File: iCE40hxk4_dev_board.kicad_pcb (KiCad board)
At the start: 4 copper layers, 66.4 x 162.5 mm, 365 parts, among them J1001 Testpoint, J1002 Testpoint, J1003 Testpoint, J1004 Testpoint, J1005 USB_EXT, J101 CONN_01X02, J102 NRJ6HM-1, J103 CONN_COAXIAL, J104 CONN_COAXIAL, J1101 CONN_01X25, J202 USB_OTG, J401 Testpoint, J402 Testpoint, J404 Testpoint, J405 Testpoint, J406 Testpoint, J501 Testpoint, J502 Testpoint, J601 CONN_01X02, J602 CONN_01X02, J603 Testpoint, J604 Testpoint, J605 Testpoint, J701 Testpoint, J703 Testpoint, J704 Testpoint, J705 Testpoint, J706 Testpoint, J801 Testpoint, J802 Testpoint, J803 Testpoint, J804 Testpoint, J805 Testpoint, J806 Testpoint, J807 Testpoint, J808 Testpoint, J809 Testpoint, J810 Testpoint, SW1101 SW_Push, U1001 ADC1175, U1002 ADC1175, U1101 MIC7300, U1102 MIC7300, U1103 MCP4716, U1104 MCP4716, U1105 MIC7300, U1106 MIC7300, U201 MIC2005A-2YM5, U203 93LC56BT-I/O, U204 MIC5355/6-xYMME, U205 FT2232H, U301 iCE40-HX4K-TQ144, U302 25LC_EEPROM, U501 AS4C1M16S, U701 CPC1017N, U702 CPC1017N, U703 CD4051BM96, U704 CD4051BM96, U801 CD4051BM96, U802 CD4051BM96, U803 CLC4007, U901 LM2776DBVR, U902 TCR2EF13, U903 MIC5270

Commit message: DRC
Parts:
- added J403, J702: Testpoint, library:TestPoint, F.Cu at (120.7, 200.2)
- J1001, J1002, J1003, J1004, J401, J402, J404, J405, J406, J501, J502, J603, J604, J605, J701, J703, J704, J705, J706, J801, J802, J803, J804, J805, J806, J807, J808, J809, J810: footprint library:Via-0.8mm -> library:TestPoint
- moved J405 136.3 mm to (102.9, 65.4)
- moved J406 126.5 mm to (107.8, 74.8)
- moved J501 115.0 mm to (137.9, 87.3)
- moved J502 111.6 mm to (102.6, 90.4)
- moved J1001 87.9 mm to (174.3, 132.6)
- moved J1002 87.9 mm to (174.3, 132.6)
- moved J1003 87.9 mm to (174.3, 132.6)
- moved J1004 87.9 mm to (174.3, 132.6)
- moved J603 87.9 mm to (174.3, 132.6)
- moved J604 87.9 mm to (174.3, 132.6)
- moved J605 87.9 mm to (174.3, 132.6)
- moved J701 87.9 mm to (174.3, 132.6)
- moved J703 87.9 mm to (174.3, 132.6)
- moved J704 87.9 mm to (174.3, 132.6)
- moved J705 87.9 mm to (174.3, 132.6)
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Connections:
- J1005 pad 2: Net-(J1005-Pad2) -> (no net)
- J1005 pad 3: Net-(J1005-Pad3) -> (no net)
- J1005 pad 4: Net-(J1005-Pad4) -> (no net)
- J202 pad 4: Net-(J202-Pad4) -> (no net)
- U1001 pad 16: Net-(U1001-Pad16) -> (no net)
- U1001 pad 22: Net-(U1001-Pad22) -> (no net)
- U1002 pad 16: Net-(U1002-Pad16) -> (no net)
- U1002 pad 22: Net-(U1002-Pad22) -> (no net)
- U205 pad 19: Net-(U205-Pad19) -> (no net)
- U205 pad 22: Net-(U205-Pad22) -> (no net)
- U205 pad 26: Net-(U205-Pad26) -> (no net)
- U205 pad 27: Net-(U205-Pad27) -> (no net)
- U205 pad 28: Net-(U205-Pad28) -> (no net)
- U205 pad 29: Net-(U205-Pad29) -> (no net)
- U205 pad 3: Net-(U205-Pad3) -> (no net)
- U205 pad 30: Net-(U205-Pad30) -> (no net)
- U205 pad 32: Net-(U205-Pad32) -> (no net)
- U205 pad 33: Net-(U205-Pad33) -> (no net)
- U205 pad 34: Net-(U205-Pad34) -> (no net)
- U205 pad 36: Net-(U205-Pad36) -> (no net)
- U205 pad 57: Net-(U205-Pad57) -> (no net)
- U205 pad 58: Net-(U205-Pad58) -> (no net)
- U205 pad 59: Net-(U205-Pad59) -> (no net)
- U205 pad 60: Net-(U205-Pad60) -> (no net)
- U301 pad 109: Net-(U301-Pad109) -> (no net)
- U301 pad 133: Net-(U301-Pad133) -> (no net)
- U301 pad 35: Net-(U301-Pad35) -> (no net)
- U301 pad 36: Net-(U301-Pad36) -> (no net)
- U301 pad 50: Net-(U301-Pad50) -> (no net)
- U301 pad 51: Net-(U301-Pad51) -> (no net)
- U301 pad 58: Net-(U301-Pad58) -> (no net)
- U301 pad 77: Net-(U301-Pad77) -> (no net)
- U501 pad 33: Net-(U501-Pad33) -> (no net)
- U501 pad 37: Net-(U501-Pad37) -> (no net)
- U902 pad 4: Net-(U902-Pad4) -> (no net)
- U903 pad 1: Net-(U903-Pad1) -> (no net)
- U903 pad 3: Net-(U903-Pad3) -> (no net)
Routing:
- net (no net): track 6.10 -> 0.19 mm
- net GND: track 1645.2 -> 1640.3 mm
- net +3V3: track 502.7 -> 498.3 mm
- net Net-(U205-Pad28): track 4.20 -> 0.00 mm
- net Net-(U205-Pad27): track 3.50 -> 0.00 mm
- net Net-(U205-Pad26): track 2.60 -> 0.00 mm
- net /Analog front end/ATTENUATION/CHB_ATT_40dB: track 36.0 -> 34.0 mm
- net /Analog front end/ATTENUATION/CHB_ATT_20dB: track 51.0 -> 49.2 mm
- net /Analog front end/CHB_PGA_OUT: track 45.4 -> 46.9 mm
- net /Analog front end/CHA_ATT_OUT: track 42.5 -> 43.8 mm
- net /Analog front end/CHB_ATT_OUT: track 57.3 -> 58.5 mm
- net /Analog front end/CHA_PGA_OUT: track 66.6 -> 67.3 mm

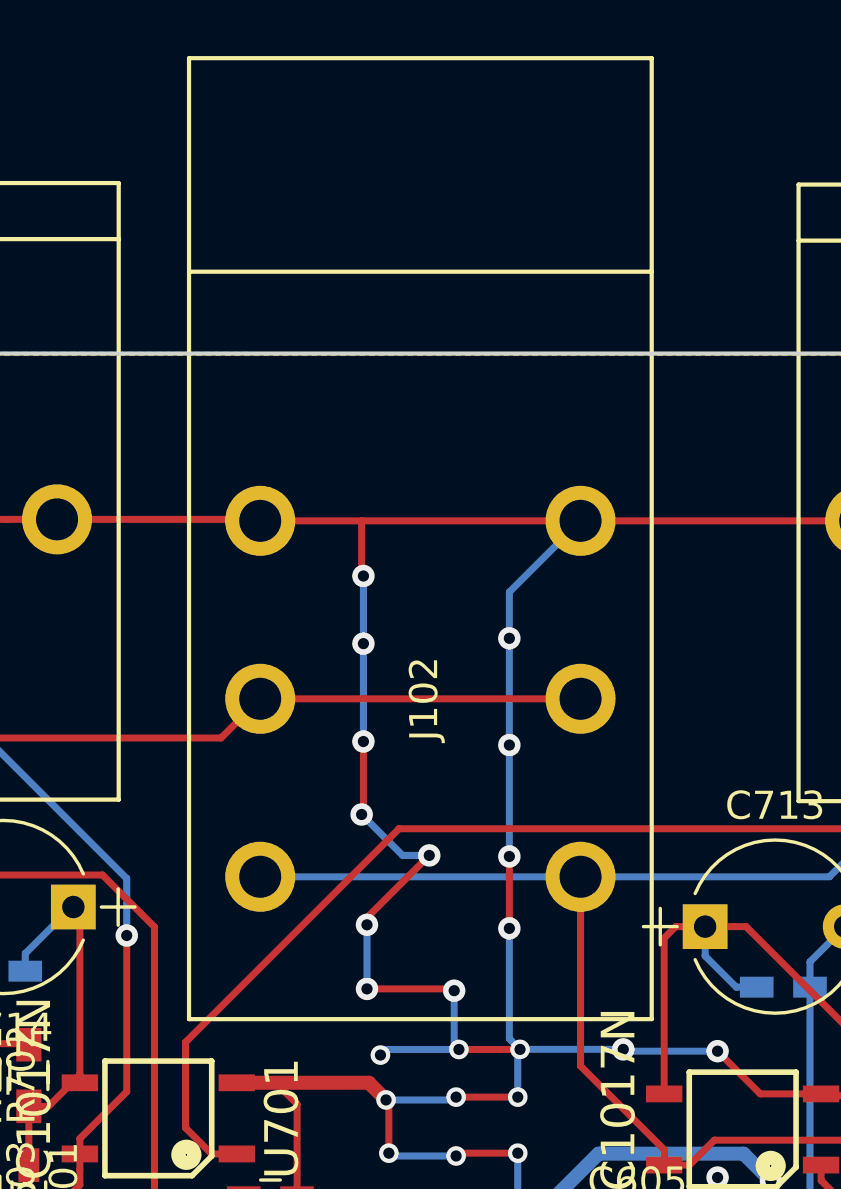
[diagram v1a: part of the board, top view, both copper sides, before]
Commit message: Changed 1/4 jack to 1/8 jack
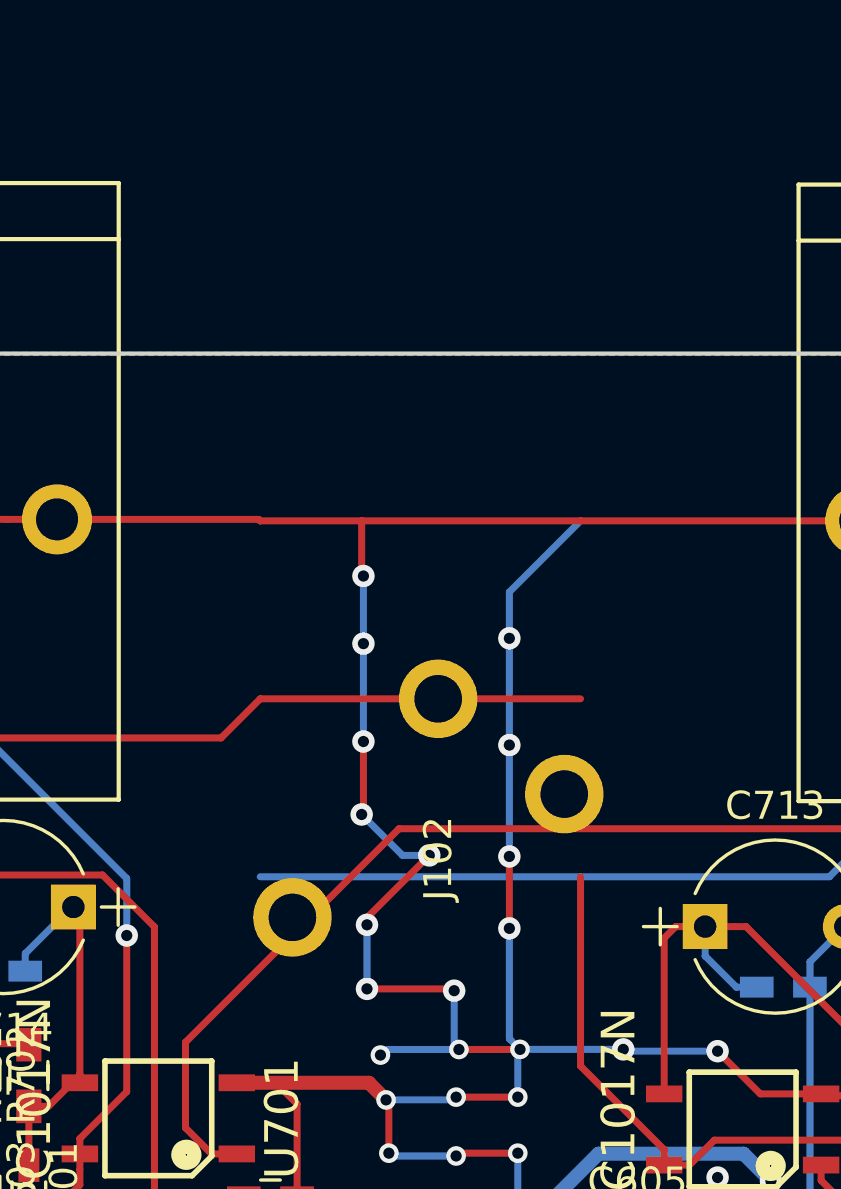
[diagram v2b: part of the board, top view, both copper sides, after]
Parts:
- J102: value NRJ6HM-1 -> KobiConn_161-3507_Jack_3.5mm; footprint library:NRJ6HM-1_audio_jack -> library:KobiConn_161-3507_Jack_3.5mm
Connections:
- J1005 pad 2: (no net) -> Net-(J1005-Pad2)
- J1005 pad 3: (no net) -> Net-(J1005-Pad3)
- J1005 pad 4: (no net) -> Net-(J1005-Pad4)
- J102 pad 2: /CHB -> /CHA
- J102 pad 3: /CHA -> /CHB
- J202 pad 4: (no net) -> Net-(J202-Pad4)
- U1001 pad 16: (no net) -> Net-(U1001-Pad16)
- U1001 pad 22: (no net) -> Net-(U1001-Pad22)
- U1002 pad 16: (no net) -> Net-(U1002-Pad16)
- U1002 pad 22: (no net) -> Net-(U1002-Pad22)
- U205 pad 19: (no net) -> Net-(U205-Pad19)
- U205 pad 22: (no net) -> Net-(U205-Pad22)
- U205 pad 26: (no net) -> Net-(U205-Pad26)
- U205 pad 27: (no net) -> Net-(U205-Pad27)
- U205 pad 28: (no net) -> Net-(U205-Pad28)
- U205 pad 29: (no net) -> Net-(U205-Pad29)
- U205 pad 3: (no net) -> Net-(U205-Pad3)
- U205 pad 30: (no net) -> Net-(U205-Pad30)
- U205 pad 32: (no net) -> Net-(U205-Pad32)
- U205 pad 33: (no net) -> Net-(U205-Pad33)
- U205 pad 34: (no net) -> Net-(U205-Pad34)
- U205 pad 36: (no net) -> Net-(U205-Pad36)
- U205 pad 57: (no net) -> Net-(U205-Pad57)
- U205 pad 58: (no net) -> Net-(U205-Pad58)
- U205 pad 59: (no net) -> Net-(U205-Pad59)
- U205 pad 60: (no net) -> Net-(U205-Pad60)
- U301 pad 109: (no net) -> Net-(U301-Pad109)
- U301 pad 133: (no net) -> Net-(U301-Pad133)
- U301 pad 35: (no net) -> Net-(U301-Pad35)
- U301 pad 36: (no net) -> Net-(U301-Pad36)
- U301 pad 50: (no net) -> Net-(U301-Pad50)
- U301 pad 51: (no net) -> Net-(U301-Pad51)
- U301 pad 58: (no net) -> Net-(U301-Pad58)
- U301 pad 77: (no net) -> Net-(U301-Pad77)
- U501 pad 33: (no net) -> Net-(U501-Pad33)
- U501 pad 37: (no net) -> Net-(U501-Pad37)
- U902 pad 4: (no net) -> Net-(U902-Pad4)
- U903 pad 1: (no net) -> Net-(U903-Pad1)
- U903 pad 3: (no net) -> Net-(U903-Pad3)

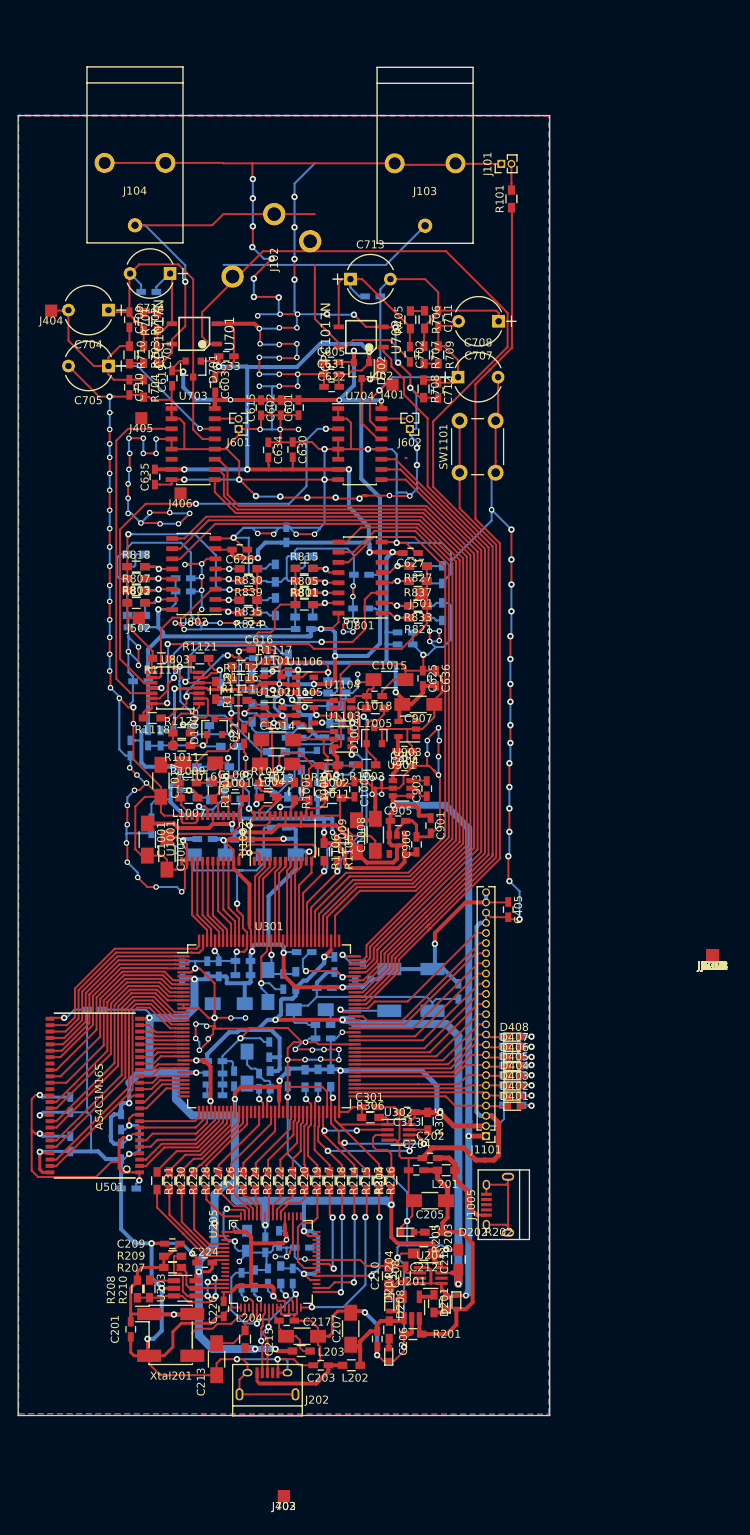
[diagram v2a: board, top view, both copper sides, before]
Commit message: Changed audio jack in pcb
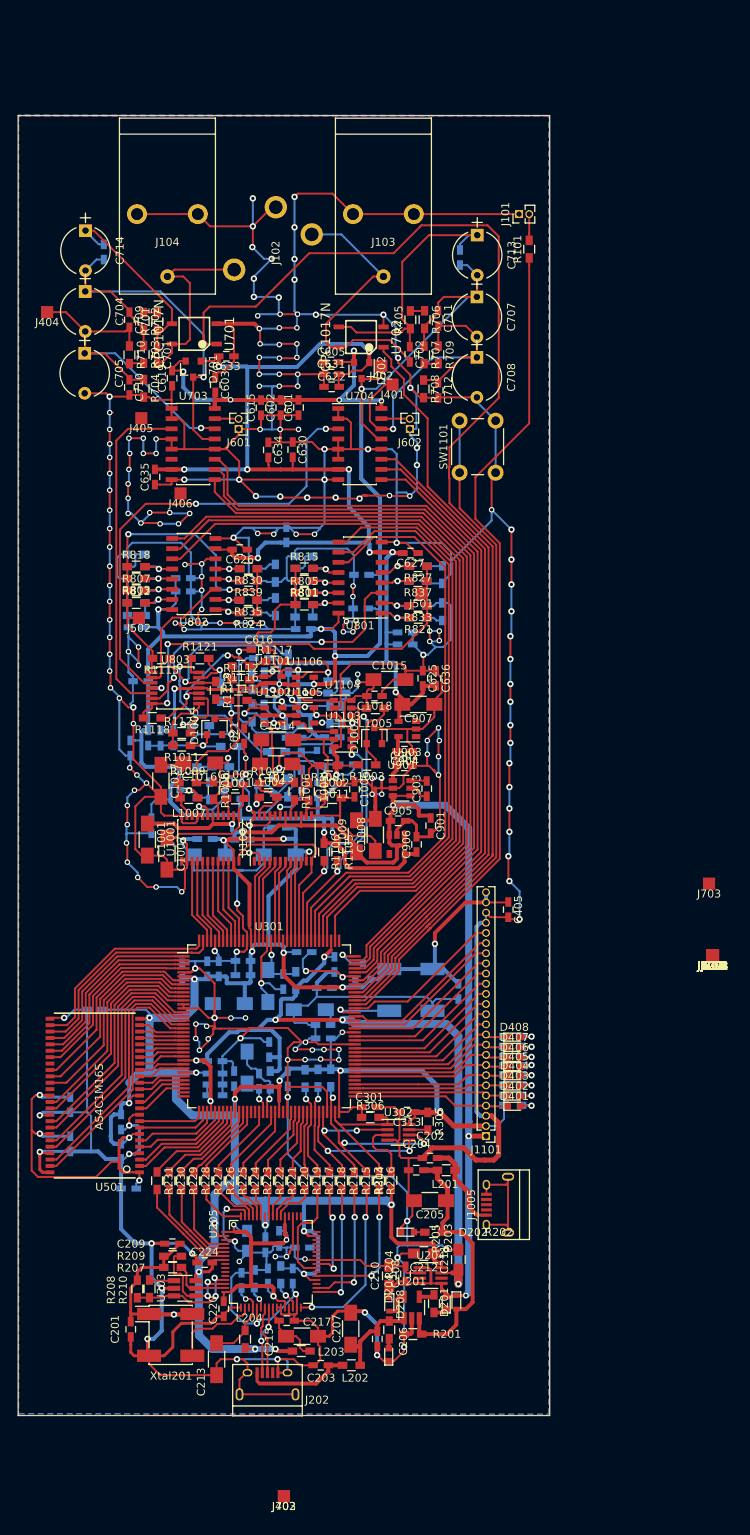
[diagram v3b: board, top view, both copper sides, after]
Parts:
- moved C713 16.8 mm to (144.9, 42.5), turned to 270 degrees
- moved C706 11.9 mm to (142.7, 45.3), turned to 270 degrees
- moved C714 11.9 mm to (95.9, 42.0), turned to 270 degrees
- moved J703 9.01 mm to (173.8, 123.6)
- moved J103 8.21 mm to (133.1, 43.9)
- moved J104 7.58 mm to (106.1, 43.9)
- moved C703 7.51 mm to (98.2, 44.6), turned to 270 degrees
- moved J101 6.67 mm to (150.1, 39.9)
- moved R101 6.67 mm to (151.4, 44.3)
- moved C707 4.08 mm to (144.8, 50.3), turned to 270 degrees
- moved C704 3.73 mm to (95.9, 49.6), turned to 270 degrees
- moved C708 3.41 mm to (144.8, 57.8), turned to 270 degrees
- moved C705 3.37 mm to (95.8, 57.3), turned to 270 degrees
- moved J102 0.88 mm to (119.7, 39.1)
- moved J404 0.54 mm to (91.1, 52.2)
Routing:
- net /CHA: track 45.4 -> 24.8 mm, vias 1 -> 0
- net /CHB: track 49.3 -> 35.5 mm
- net Net-(C702-Pad1): track 23.0 -> 34.6 mm
- net /Analog front end/ATTENUATION/CHB_ATT_40dB: track 34.0 -> 44.9 mm
- net Net-(C701-Pad1): track 13.8 -> 24.5 mm
- net GND: track 1640.3 -> 1631.9 mm, vias 222 -> 220
- net /Analog front end/CHA_DC_COUPLING: track 150.3 -> 155.7 mm
- net /RIGHT_TOP_BANKs/IOT_146: track 111.8 -> 106.4 mm
- net /Analog front end/ATTENUATION/CHA_ATT_40dB: track 41.6 -> 46.1 mm
- net /Analog front end/ATTENUATION/CHA_ATT_20dB: track 46.6 -> 50.6 mm, vias 0 -> 1
